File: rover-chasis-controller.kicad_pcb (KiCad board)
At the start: 2 copper layers, 100 x 100 mm, 78 parts, among them J1 Motor control, J11 Compass Connection (I2C), J15 External LED (Red), J16 External LED (Yellow), J17 External LED (Green), J2 Motor control, J22 Ultrasonic Sensor Inputs, J3 Motor control, J38 Motor control, J4 Screw_Terminal_01x02, J40 Encoder, J41 Encoder, J42 Encoder, J43 Encoder, J7 TTL, J8 Ultrasonic Sensor Inputs, Q14 MMBT3904_C181119, Q2 HSBA100P04_C2987717, Q33 MMBT3904_C181119, Q34 MMBT3904_C181119, Q35 MMBT3904_C181119, U1 APT2012LVBC/D, U2 APT2012LVBC/D, U3 APT2012LVBC/D, U4 AP64500, U5 MPU-6050_C24112, U6 PCA9685PW,118, U7 APT2012LVBC/D

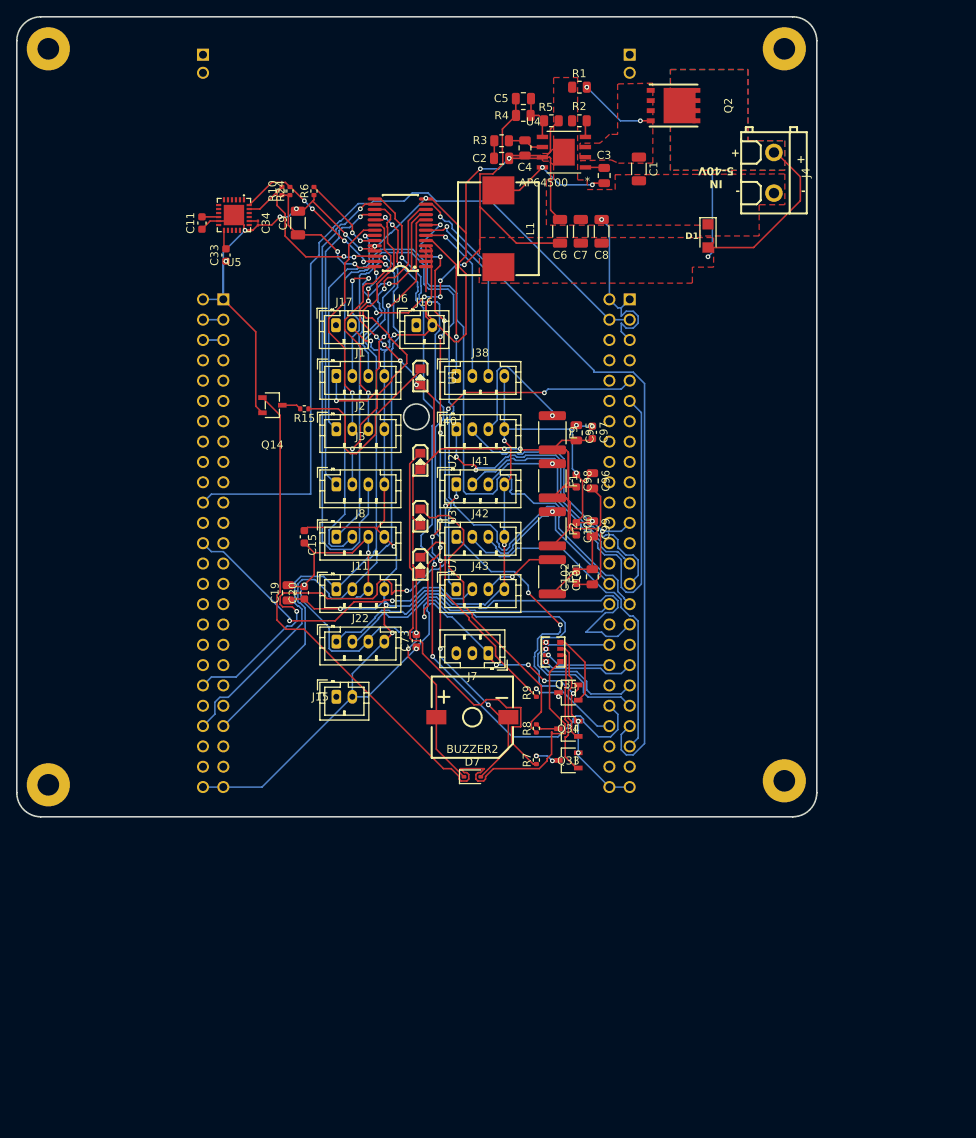
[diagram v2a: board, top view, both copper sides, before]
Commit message: Issue #1: Refactored PCB design
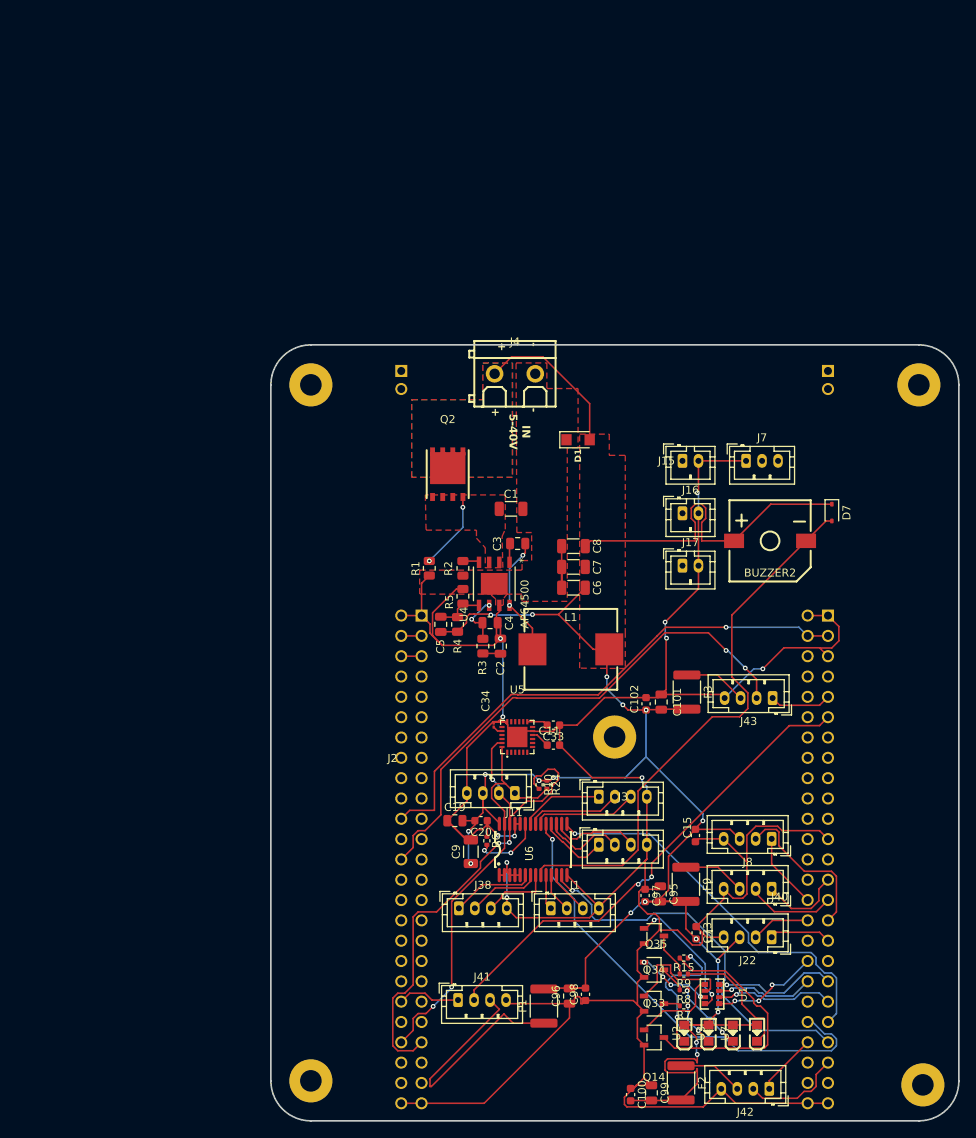
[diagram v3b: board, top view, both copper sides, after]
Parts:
- removed the MK1 at (96.0, 4.00)
- removed the MK1 at (4.00, 4.00)
- removed the MK1 at (96.0, 95.5)
- removed the MK1 at (4.00, 96.0)
- added MK1: M2.5, MountingHole:MountingHole_2.7mm_M2.5_Pad, F.Cu at (113.3, 133.5)
- added MK1: M2.5, MountingHole:MountingHole_2.7mm_M2.5_Pad, F.Cu at (112.8, 46.0)
- added MK1: M2.5, MountingHole:MountingHole_2.7mm_M2.5_Pad, F.Cu at (74.8, 90.0)
- added MK1: M2.5, MountingHole:MountingHole_2.7mm_M2.5_Pad, F.Cu at (36.8, 46.0)
- added MK1: M2.5, MountingHole:MountingHole_2.7mm_M2.5_Pad, F.Cu at (36.8, 133.0)
- moved Q14 92.3 mm to (79.7, 127.6)
- moved U1 88.4 mm to (83.5, 127.0), turned to 90 degrees
- moved R6 84.0 mm to (58.8, 103.0), turned to -90 degrees
- moved R15 83.4 mm to (83.4, 117.7)
- moved C9 81.5 mm to (56.8, 104.4)
- moved R10 80.9 mm to (65.3, 96.0), turned to -90 degrees
- moved R24 80.9 mm to (66.3, 96.0), turned to -90 degrees
- moved U2 80.0 mm to (86.5, 127.0), turned to 90 degrees
- moved J42 79.3 mm to (94.1, 134.0), turned to 180 degrees
- moved U6 78.9 mm to (64.6, 104.1), turned to 90 degrees
- moved C11 78.7 mm to (67.1, 91.0), turned to 180 degrees
- moved U3 75.4 mm to (89.6, 127.0), turned to 90 degrees
- moved U5 74.2 mm to (62.6, 90.0), turned to 0 degrees
- moved U7 72.0 mm to (92.6, 127.0), turned to 90 degrees
- moved J1 71.7 mm to (66.8, 111.4)
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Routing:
- net /US_SENSOR1_TRIG: track 109.5 -> 9.51 mm
- net /US_SENSOR1_ECHO: track 115.5 -> 20.0 mm
- net /transistor_array4/B1: track 94.7 -> 11.2 mm
- net /LED_GREEN: track 102.2 -> 49.0 mm, vias 3 -> 1
- net /ENC2_A: track 56.2 -> 7.89 mm, vias 4 -> 0
- net /MOTOR4_RVR: track 59.0 -> 11.1 mm, vias 1 -> 0
- net /SDA: track 98.7 -> 51.5 mm, vias 5 -> 2
- net Net-(U2-K): track 52.4 -> 5.51 mm, vias 0 -> 2
- net /US_SENSOR2_TRIG: track 52.2 -> 7.74 mm
- net /LED_RED: track 89.5 -> 47.6 mm
- net /ENC3_A: track 47.7 -> 7.73 mm, vias 2 -> 0
- net /LED_YELLOW: track 94.4 -> 58.7 mm, vias 5 -> 1
- net /SCL: track 102.1 -> 67.9 mm
- net /MOTOR4_FWD: track 43.8 -> 10.3 mm, vias 1 -> 0
- net /ENC4_A: track 39.1 -> 7.81 mm, vias 2 -> 0
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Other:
- board size 100 x 100 mm -> 86 x 97 mm

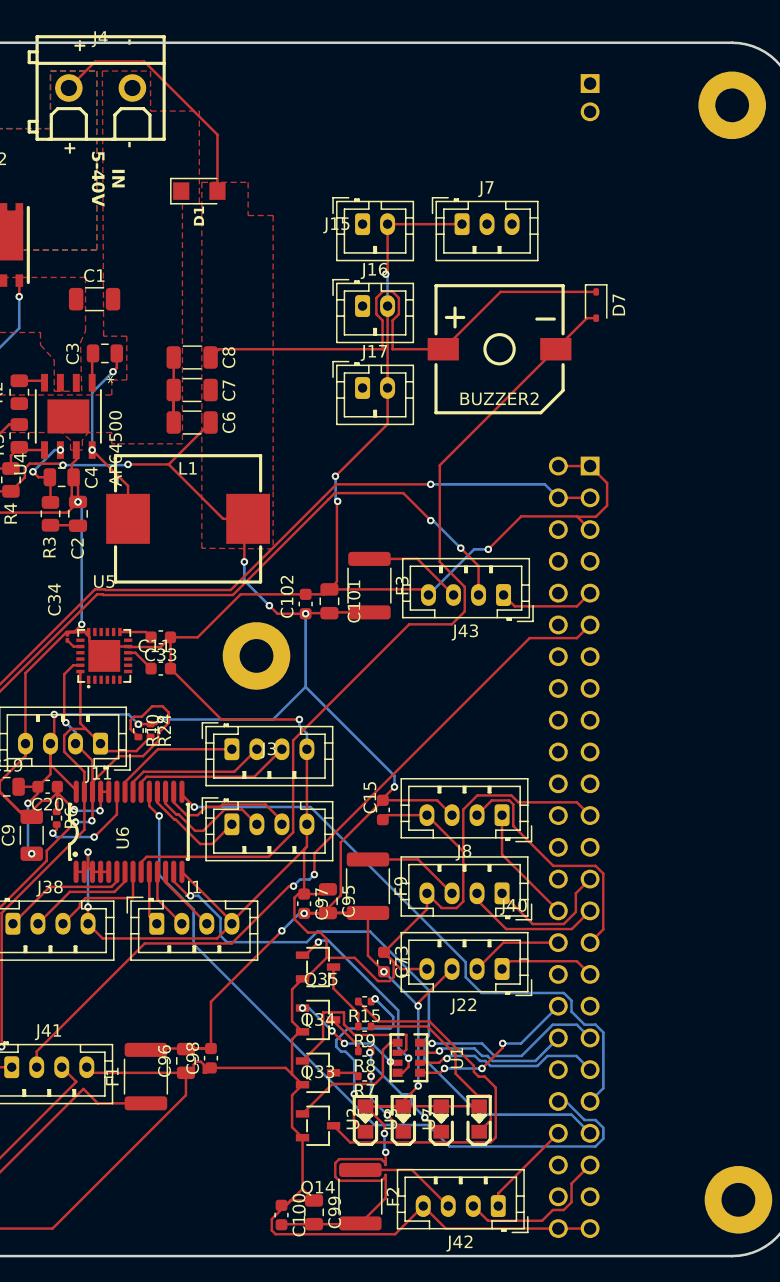
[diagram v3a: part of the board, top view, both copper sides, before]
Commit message: Issue #1: Corrected some mistakes
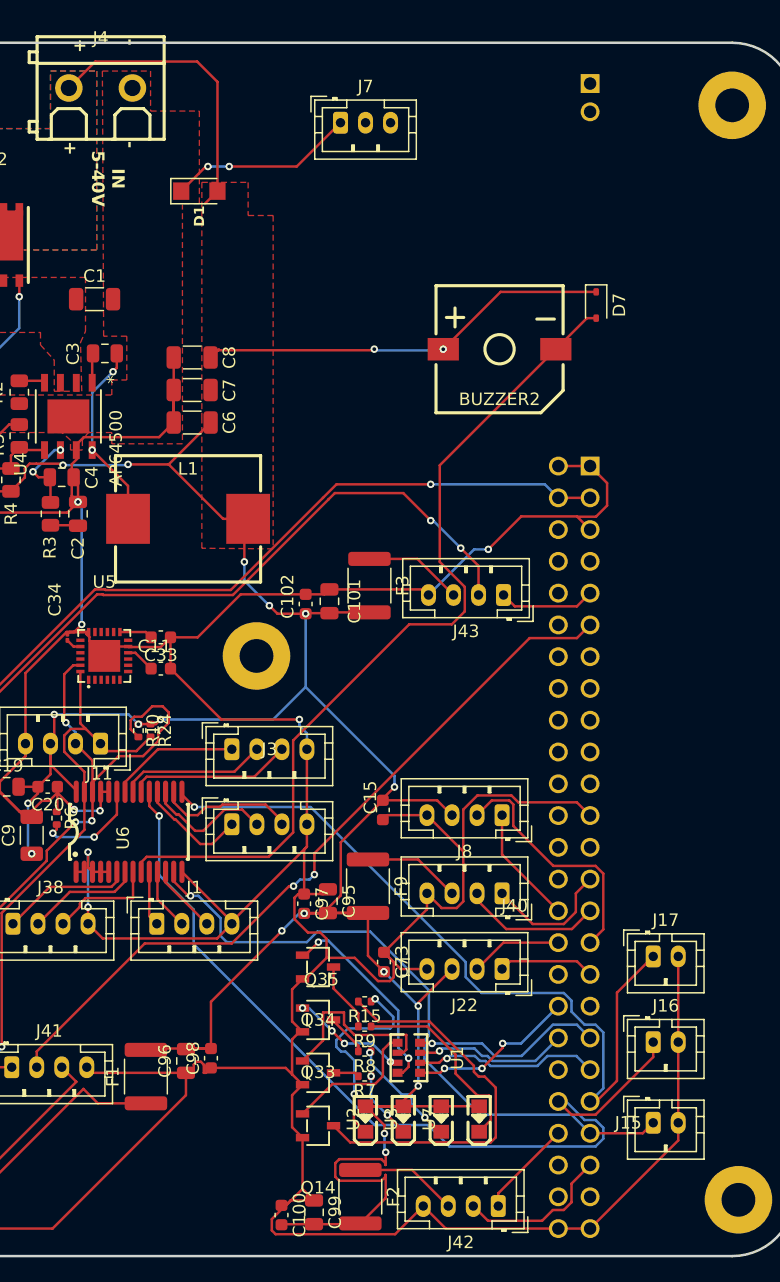
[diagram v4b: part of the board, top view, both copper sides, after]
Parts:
- moved J15 75.5 mm to (106.5, 127.3)
- moved J16 63.3 mm to (106.5, 120.9)
- moved J17 51.0 mm to (106.5, 114.0)
- moved J7 12.7 mm to (81.5, 47.4)
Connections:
- J15 pad 1: /External_LED_Collector_1 -> /LED_RED
- J16 pad 1: /External_LED_Collector_2 -> /LED_YELLOW
- J17 pad 1: /External_LED_Collector_3 -> /LED_GREEN
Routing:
- net /LED_GREEN: track 49.0 -> 62.9 mm
- net GND: track 412.3 -> 423.6 mm, vias 11 -> 10
- net /LED_YELLOW: track 58.7 -> 69.8 mm
- net VCC (5V): track 274.4 -> 268.5 mm, vias 18 -> 20
- net /LED_RED: track 47.6 -> 53.0 mm

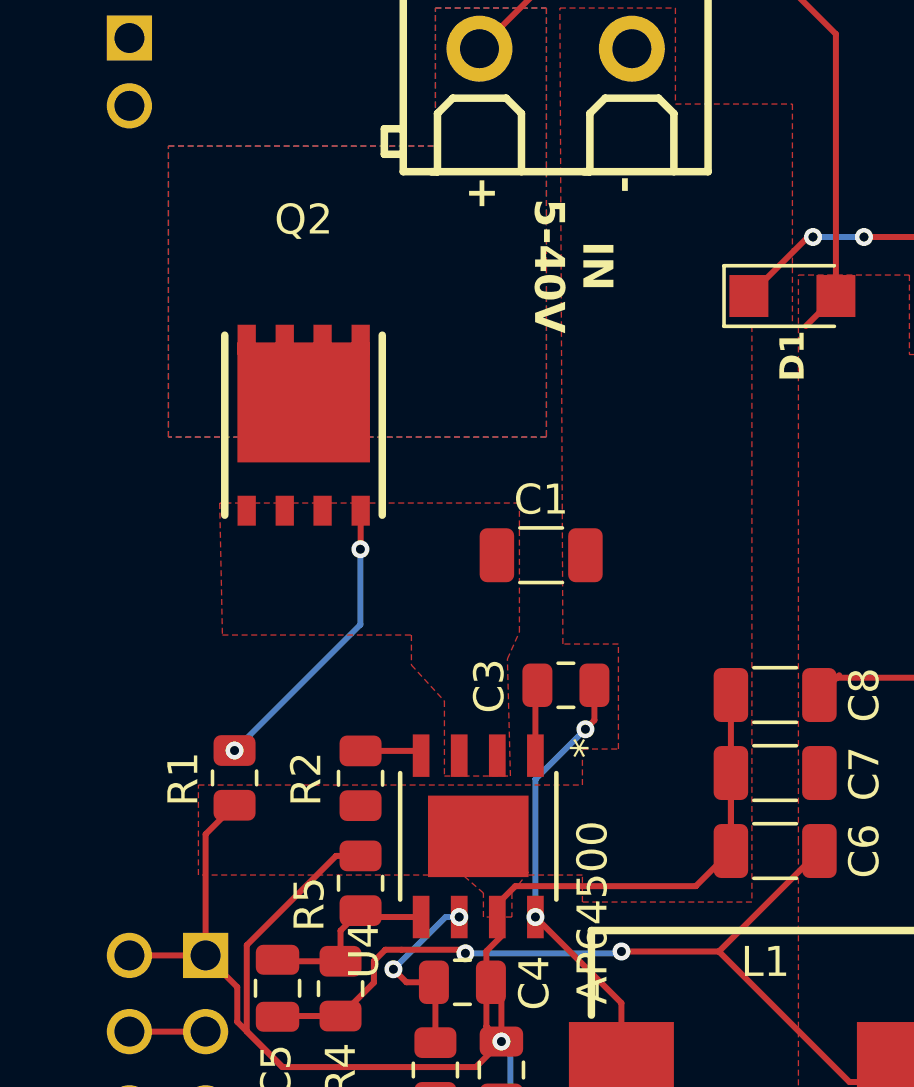
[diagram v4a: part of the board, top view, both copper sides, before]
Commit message: Issue #1: Improved power supply zoning
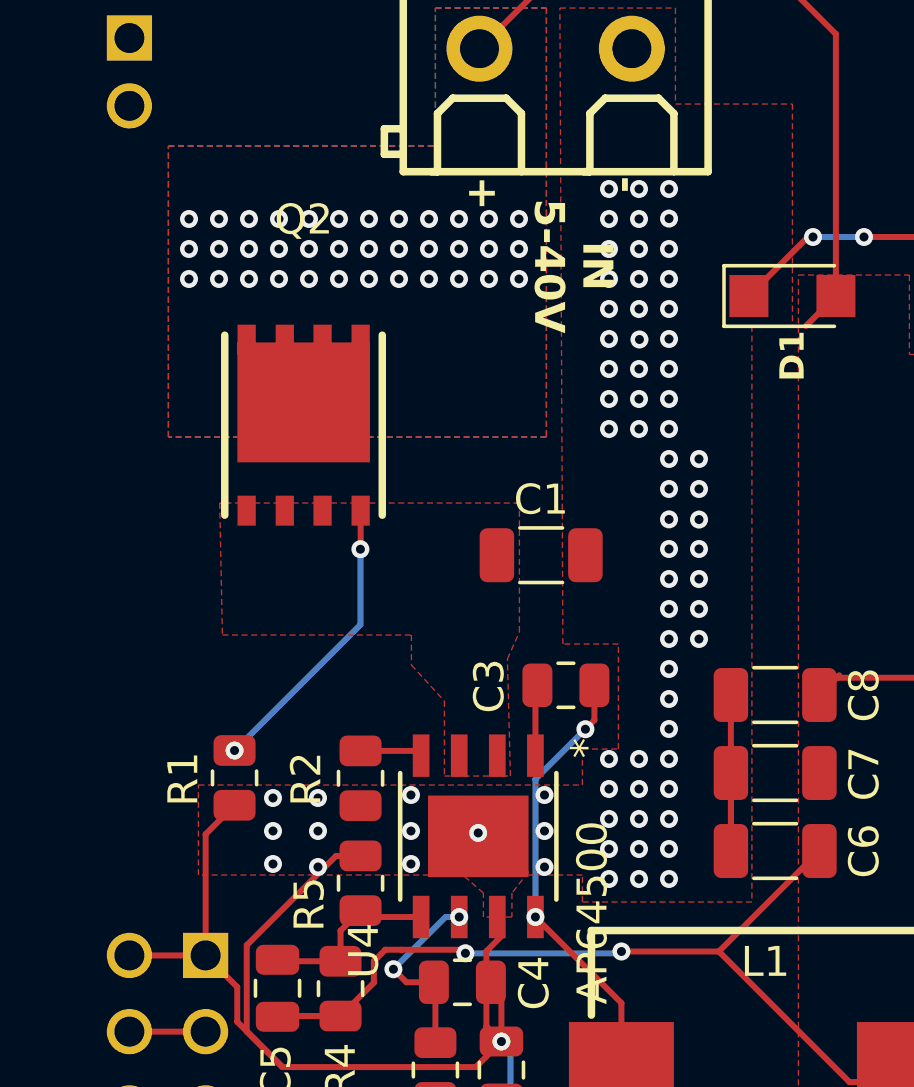
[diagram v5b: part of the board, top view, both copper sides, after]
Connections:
- U4 pad EPAD: (no net) -> GND
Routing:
- net GND: track 423.6 -> 415.1 mm, vias 10 -> 82
- net VCC (5V): vias 20 -> 56
